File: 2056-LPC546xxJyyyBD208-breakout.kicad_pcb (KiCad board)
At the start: 2 copper layers, 99.1 x 99.1 mm, 149 parts, among them J1 0548190519, J10 Conn_01x03, J11 Conn_01x03, J12 Conn_01x03, J13 Conn_01x03, J14 Conn_01x03, J15 Conn_01x03, J16 Conn_01x03, J17 Conn_01x03, J18 Conn_01x03, J19 Conn_01x03, J2 Conn_01x03, J20 Conn_01x03, J21 Conn_01x03, J22 Conn_01x03, J23 Conn_01x03, J24 Conn_01x03, J25 Conn_01x03, J26 Conn_01x03, J27 Conn_01x03, J28 Conn_01x03, J29 Conn_01x03, J3 Conn_01x03, J30 Conn_02x01, J31 Conn_01x03, J32 Conn_01x04, J33 Conn_01x03, J34 TBL001-500-02GY-2GY, J35 Conn_02x05_Odd_Even, J36 Conn_01x03, J37 Conn_02x20_Odd_Even, J38 Conn_01x03, J39 Conn_01x03, J4 Conn_01x03, J40 Conn_01x03, J41 Conn_01x03, J42 Conn_01x03, J43 Conn_01x03, J5 Conn_01x03, J6 Conn_01x03, J7 Conn_01x03, J8 Conn_01x03, J9 Conn_01x03, Q2 ULN2803ADWR, Q3 ULN2803ADWR, SW1 SW_DIP_x08, U1 ST3232ECDR‎, U2 LPC546xxJyyyBD208, U3 SN65HVD232, U4 FAN8303, U5 FAN8303, U6 NCP1117ST50T3G, U7 FAN8303, Y1 12MHz

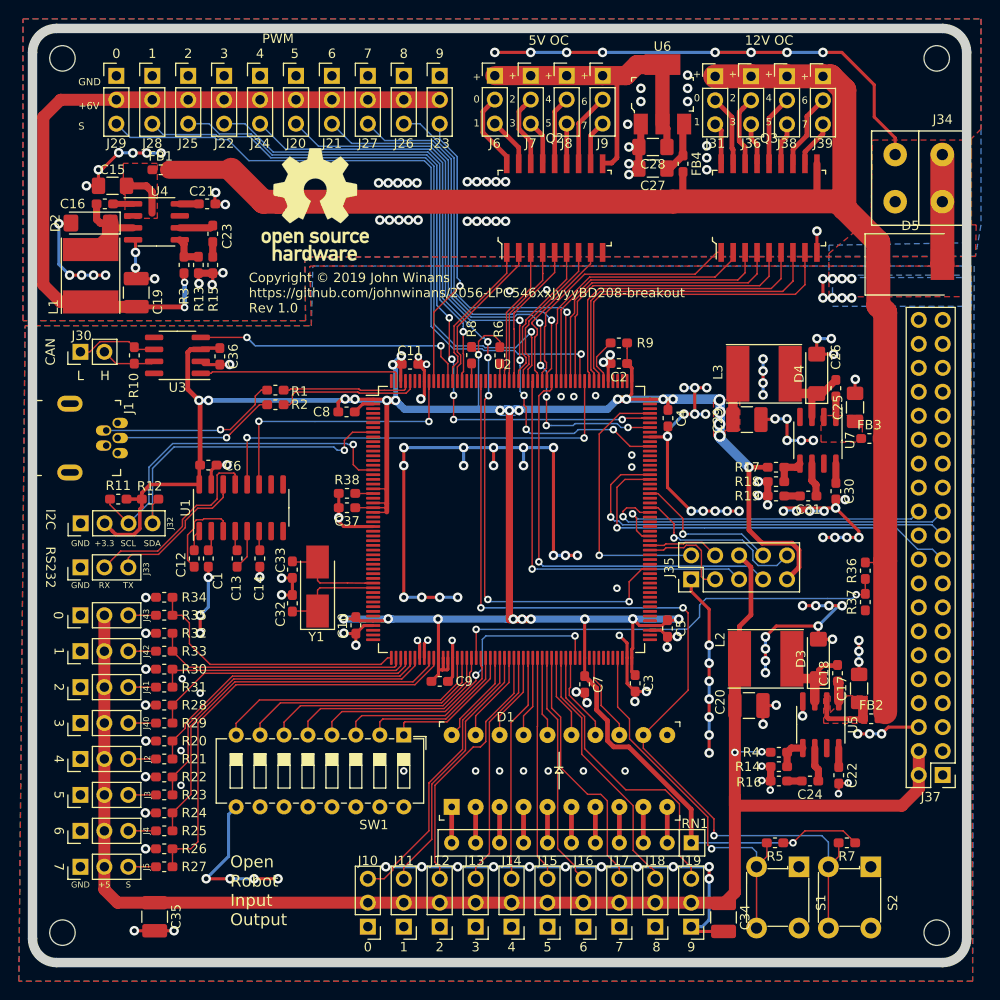
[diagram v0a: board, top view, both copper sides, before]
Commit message: Cosmetic silkscreen & title block cleanup.
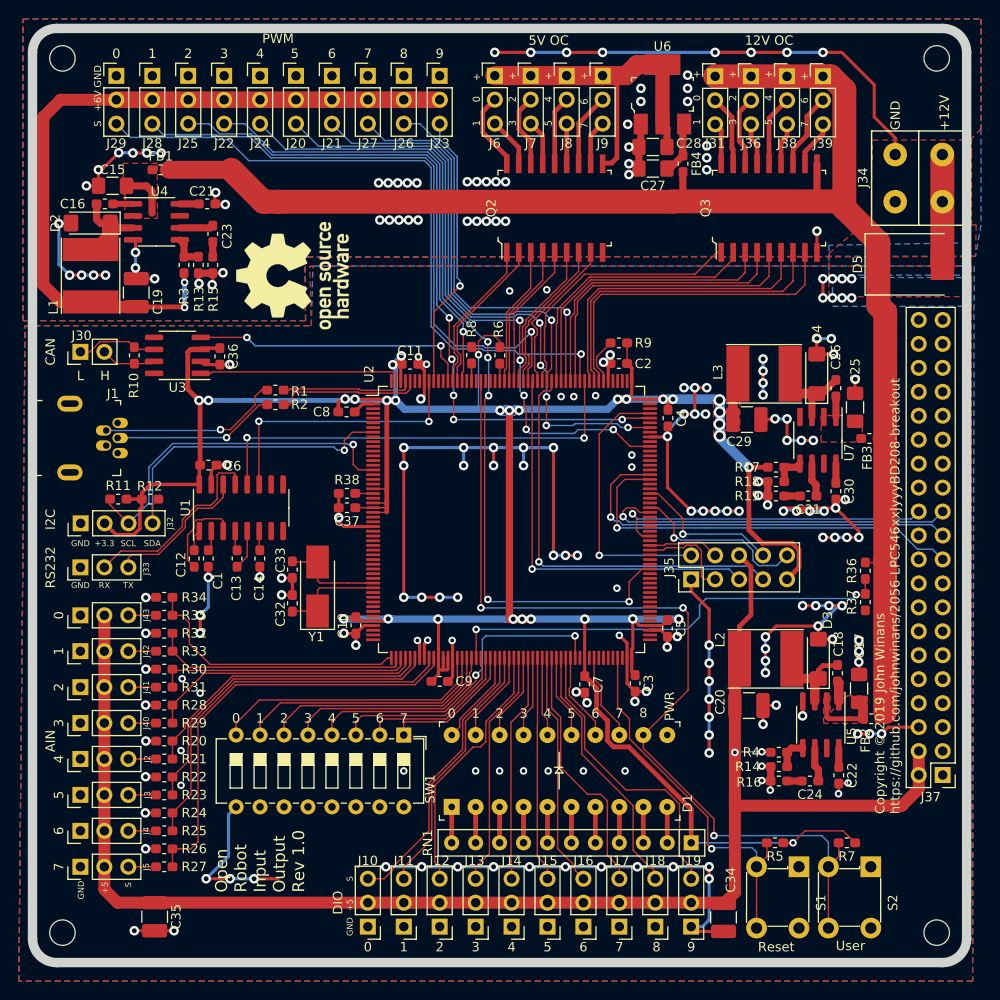
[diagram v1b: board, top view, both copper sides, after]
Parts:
- moved LOGO1 7.93 mm to (103.8, 77.0), turned to 90 degrees
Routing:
- net GND: vias 223 -> 222
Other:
- board text added: "+12V"
- board text added: "AIN"
- board text added: "Copyright © 2019 John Winans https://github.com/johnwinans/2056-LPC546xxJyyyBD208-breakout"
- board text added: "DIO"
- board text added: "Open Robot Input Output Rev 1.0"
- board text added: "PWR"
- board text added: "Reset"
- board text added: "User"
- board text removed: "Copyright © 2019 John Winans https://github.com/johnwinans/2056-LPC546xxJyyyBD208-breakout Rev 1.0"
- board text removed: "Open Robot Input Output"

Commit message: Rev 1.1 first manufacturable draft.
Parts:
- C23: value 146pF -> 390pF
- C24: value 146pF -> 560pF
- C31: value 146pF -> 820pF
- C32, C33: value 27pF -> 12pF
- L1, L2: value 15uH -> 22uH; footprint Inductor_SMD:L_Taiyo-Yuden_NR-60xx_HandSoldering -> Inductor_SMD:L_Taiyo-Yuden_NR-80xx_HandSoldering
- R13: value X -> 3K
- R14: value X -> 2K45
- R15: value 145K -> 56K
- R16: value 145K -> 43K
- R17, R3, R4: value X -> 18K
- R18: value X -> 4K
- R19: value 145K -> 27K
- U1: value ST3232ECDR‎ -> ST3232ECDR
- U2: value LPC546xxJyyyBD208 -> LPC54606J512BD208
- moved LOGO1 5.67 mm to (109.3, 78.0)
- moved C16 3.52 mm to (87.0, 67.9)
- moved C19 3.52 mm to (90.4, 77.3)
- moved C21 3.52 mm to (97.9, 67.9)
- moved C23 3.52 mm to (98.5, 71.1)
- moved D2 3.52 mm to (85.5, 69.9)
- moved FB1 3.52 mm to (93.0, 64.3)
- moved U4 3.52 mm to (92.5, 69.8)
- moved C15 3.52 mm to (87.9, 66.0)
- moved R13 3.52 mm to (97.0, 74.4)
- moved R15 3.52 mm to (98.5, 74.4)
- moved R3 3.52 mm to (95.4, 74.4)
- moved L1 2.17 mm to (84.5, 76.5)
- moved L2 1.49 mm to (152.9, 116.6)
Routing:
- net GND: track 448.1 -> 439.9 mm, vias 222 -> 219
- net +6V: track 79.5 -> 81.6 mm
- net +BATT: track 164.6 -> 163.4 mm
- net Net-(C21-Pad1): vias 0 -> 1
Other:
- board text added: "Open Robot Input Output Rev 1.1"
- board text removed: "Open Robot Input Output Rev 1.0"

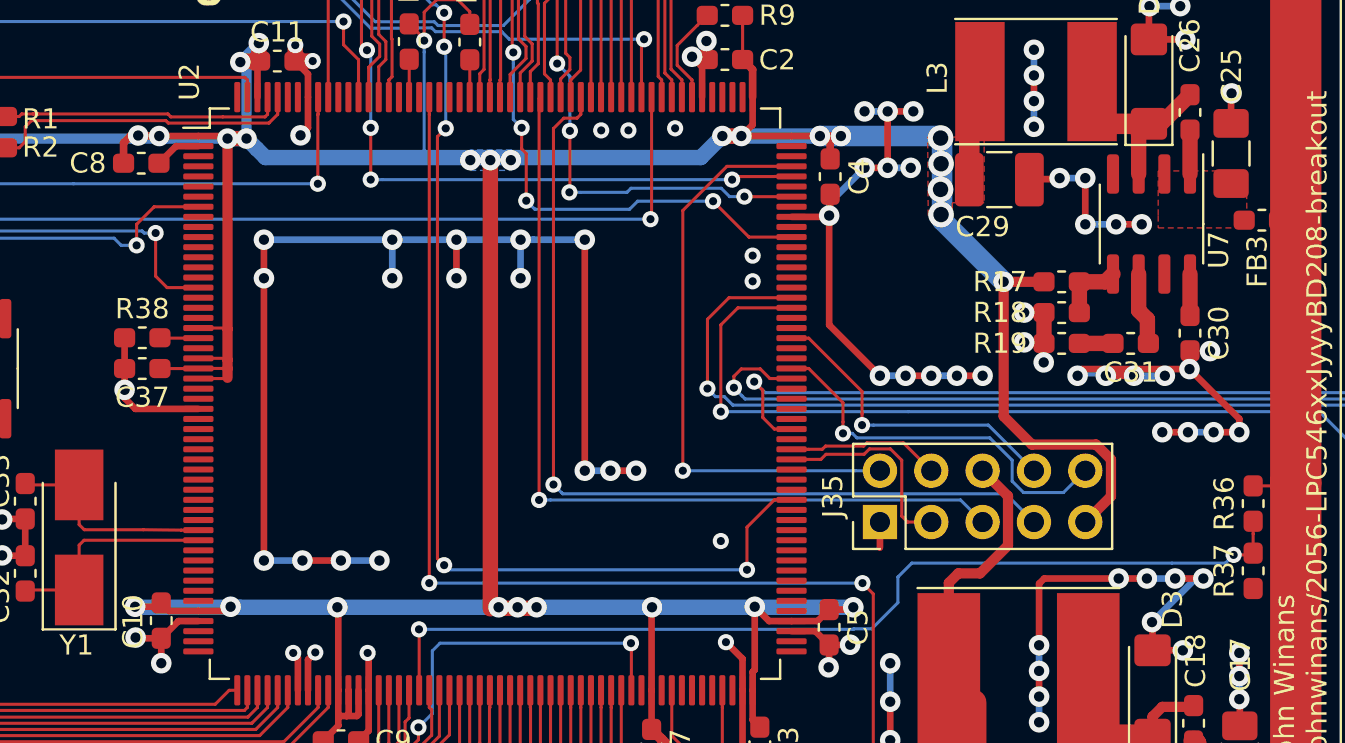
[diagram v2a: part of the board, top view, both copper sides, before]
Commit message: Correct CPU AVSSC pin.
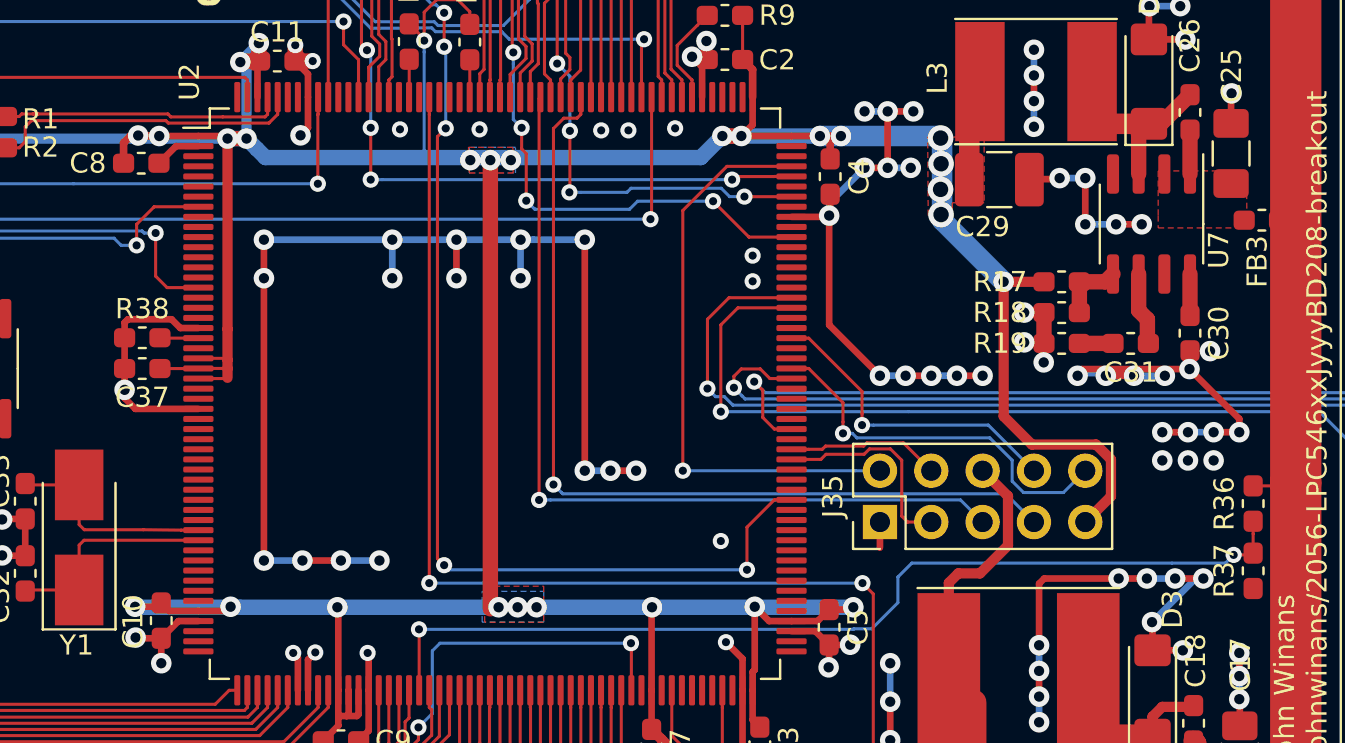
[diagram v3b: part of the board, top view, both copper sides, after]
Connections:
- U2 pad 20: +3V3 -> GND
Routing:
- net GND: track 439.9 -> 445.1 mm, vias 219 -> 224
- net +3V3: track 320.8 -> 317.1 mm
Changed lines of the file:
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@@
     (thickness 1.6)
     (drawings 115)
-    (tracks 1809)
+    (tracks 1817)
     (zones 0)
     (modules 149)
@@
     (pcbplotparams
       (layerselection 0x010fc_ffffffff)
-      (usegerberextensions false)
+      (usegerberextensions true)
       (usegerberattributes false)
       (usegerberadvancedattributes false)
@@
       (outputformat 1)
       (mirror false)
-      (drillshape 1)
+      (drillshape 0)
       (scaleselection 1)
-      (outputdirectory ""))
+      (outputdirectory "gerbers/"))
   )
   (net 0 "")
@@
       (net 293 "Net-(R38-Pad2)"))
     (pad 20 smd roundrect (at -14.675 -3.25) (size 1.5 0.3) (layers F.Cu F.Paste F.Mask) (roundrect_rratio 0.25)
-      (net 2 +3V3))
+      (net 1 GND))
     (pad 19 smd roundrect (at -14.675 -3.75) (size 1.5 0.3) (layers F.Cu F.Paste F.Mask) (roundrect_rratio 0.25)
       (net 244 "Net-(U2-Pad19)"))
@@
   (gr_line (start 175.26 53.34) (end 175.26 147.32) (layer Edge.Cuts) (width 1))
   (gr_line (start 78.74 50.8) (end 172.72 50.8) (layer Edge.Cuts) (width 1))
+  (via (at 162.56 106.172) (size 1.016) (drill 0.508) (layers F.Cu B.Cu) (net 1))
+  (via (at 161.29 106.172) (size 1.016) (drill 0.508) (layers F.Cu B.Cu) (net 1))
+  (via (at 160.02 106.172) (size 1.016) (drill 0.508) (layers F.Cu B.Cu) (net 1))
   (via (at 122.301 71.247) (size 1.016) (drill 0.508) (layers F.Cu B.Cu) (net 1))
   (via (at 122.301 67.056) (size 1.016) (drill 0.508) (layers F.Cu B.Cu) (net 1))
@@
   (segment (start 157.48 107.95) (end 157.48 106.1212) (width 0.508) (layer F.Cu) (net 2))
   (segment (start 152.1714 97.3328) (end 154.1666 97.3328) (width 0.508) (layer F.Cu) (net 2))
-  (segment (start 126.7996 113.4872) (end 129.0574 113.4872) (width 0.762) (layer F.Cu) (net 2))
   (segment (start 127.1792 113.4364) (end 126.46078 113.4364) (width 0.762) (layer B.Cu) (net 2))
   (segment (start 114.3762 113.4364) (end 109.2454 113.4364) (width 0.762) (layer B.Cu) (net 2))
@@
   (segment (start 113.693 101.12) (end 112.325 101.12) (width 0.1524) (layer F.Cu) (net 2))
   (segment (start 113.768 101.195) (end 113.768 101.624) (width 0.508) (layer F.Cu) (net 2))
-  (segment (start 113.717 99.62) (end 112.851 99.62) (width 0.1524) (layer F.Cu) (net 2))
   (segment (start 113.768 99.671) (end 113.717 99.62) (width 0.1524) (layer F.Cu) (net 2))
   (segment (start 113.768 90.2462) (end 113.768 99.671) (width 0.508) (layer F.Cu) (net 2))
   (segment (start 113.768 99.671) (end 113.768 101.195) (width 0.508) (layer F.Cu) (net 2))
-  (segment (start 112.851 99.62) (end 112.325 99.62) (width 0.1524) (layer F.Cu) (net 2))
+  (segment (start 112.851 99.62) (end 112.325 99.62) (width 0.1524) (layer F.Cu) (net 1))
+  (segment (start 112.325 99.62) (end 111.431 99.62) (width 0.3302) (layer F.Cu) (net 1))
+  (segment (start 111.431 99.62) (end 110.998 99.187) (width 0.3302) (layer F.Cu) (net 1))
+  (segment (start 110.998 99.187) (end 108.839 99.187) (width 0.3302) (layer F.Cu) (net 1))
+  (segment (start 108.6752 99.3508) (end 108.6752 100.1014) (width 0.3302) (layer F.Cu) (net 1))
+  (segment (start 108.839 99.187) (end 108.6752 99.3508) (width 0.3302) (layer F.Cu) (net 1))
+  (via (at 126.238 89.789) (size 0.8) (drill 0.4) (layers F.Cu B.Cu) (net 1))
+  (via (at 122.301 89.789) (size 0.8) (drill 0.4) (layers F.Cu B.Cu) (net 1))
   (segment (start 112.3196 101.6254) (end 112.325 101.62) (width 0.1524) (layer F.Cu) (net 2))
   (segment (start 110.4252 101.6254) (end 112.3196 101.6254) (width 0.1524) (layer F.Cu) (net 2))
@@
     )
   )
-  (zone (net 2) (net_name +3V3) (layer B.Cu) (hatch edge 0.508)
+  (zone (net 2) (net_name +3V3) (layer F.Cu) (hatch edge 0.508)
     (priority 2)
     (connect_pads yes (clearance 0.2032))
@@
     (polygon
       (pts
-        (xy 125.7808 90.805) (xy 125.7808 91.821) (xy 127.8382 91.821) (xy 127.8382 90.805)
+        (xy 125.6919 90.678) (xy 125.73 91.948) (xy 127.9017 91.948) (xy 127.889 90.678)
       )
     )
@@
       )
     )
+  )
+  (zone (net 2) (net_name +3V3) (layer F.Cu) (hatch edge 0.508)
+    (priority 2)
+    (connect_pads yes (clearance 0.2032))
+    (min_thickness 0.254)
+    (fill yes (arc_segments 32) (thermal_gap 0.254) (thermal_bridge_width 0.762))
+    (polygon
+      (pts
+        (xy 126.492 112.395) (xy 129.413 112.395) (xy 129.413 114.173) (xy 126.492 114.173)
+      )
+    )
+  )
+  (zone (net 2) (net_name +3V3) (layer B.Cu) (hatch edge 0.508)
+    (priority 2)
+    (connect_pads yes (clearance 0.2032))
+    (min_thickness 0.254)
+    (fill yes (arc_segments 32) (thermal_gap 0.254) (thermal_bridge_width 0.762))
+    (polygon
+      (pts
+        (xy 125.73 90.678) (xy 125.73 91.948) (xy 128.016 91.948) (xy 128.016 90.678)
+      )
+    )
+  )
+  (zone (net 2) (net_name +3V3) (layer B.Cu) (hatch edge 0.508)
+    (priority 2)
+    (connect_pads yes (clearance 0.2032))
+    (min_thickness 0.254)
+    (fill yes (arc_segments 32) (thermal_gap 0.254) (thermal_bridge_width 0.762))
+    (polygon
+      (pts
+        (xy 126.365 112.649) (xy 129.413 112.649) (xy 129.413 114.173) (xy 126.365 114.173)
+      )
+    )

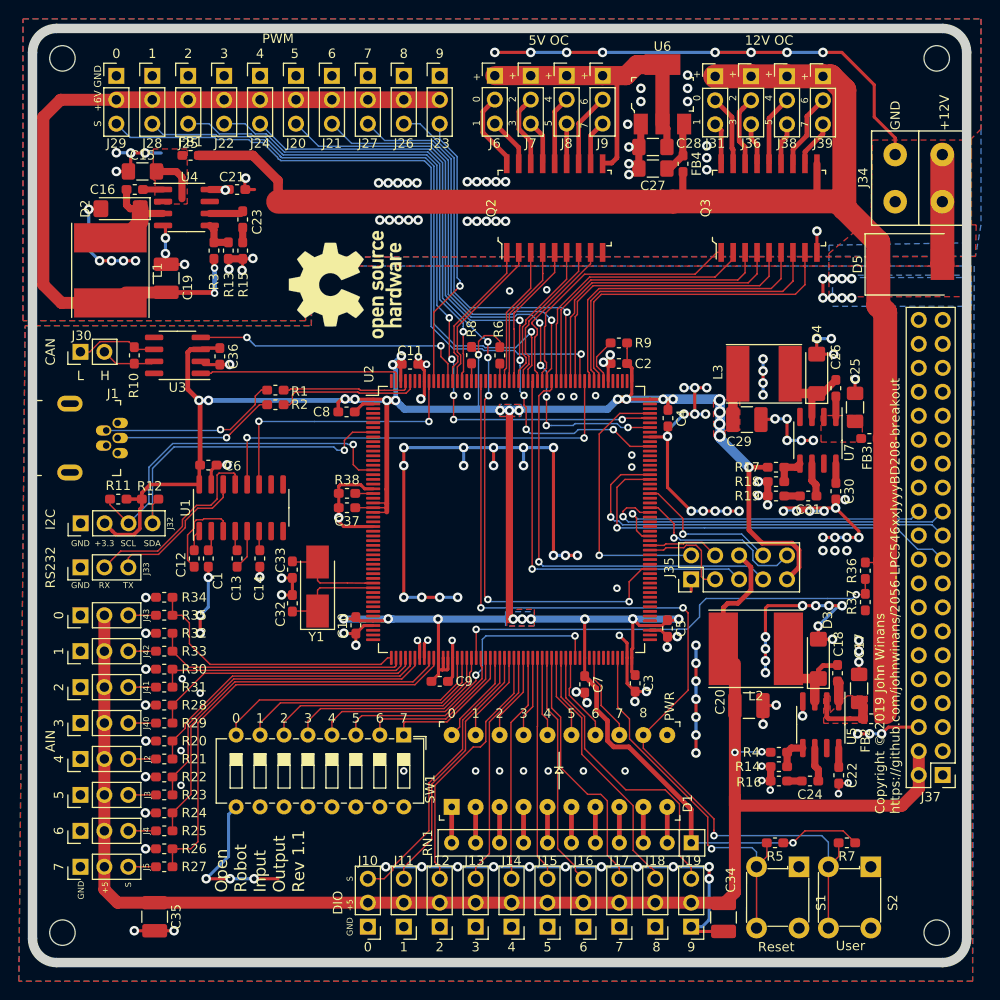
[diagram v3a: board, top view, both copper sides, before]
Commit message: Fixed power on VSSC pin, add filter caps, power & reset jumpers, SWD.
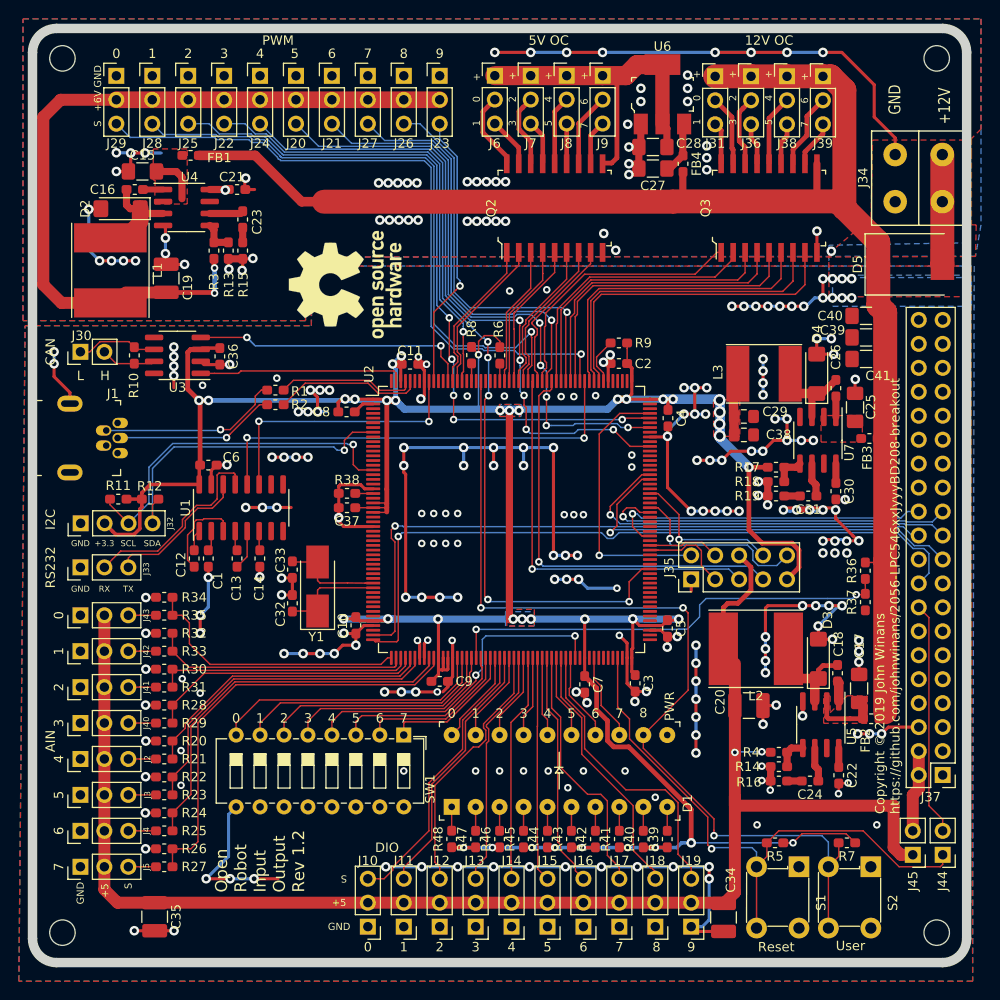
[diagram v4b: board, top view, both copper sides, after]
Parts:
- removed RN1: 330, Resistor_THT:R_Array_SIP11
- added C38: 22uF, Capacitor_SMD:C_0805_2012Metric_Pad1.15x1.40mm_HandSolder, F.Cu at (151.6, 93.9)
- added C39: 10uF, Capacitor_SMD:C_1206_3216Metric_Pad1.42x1.75mm_HandSolder, F.Cu at (164.6, 83.6)
- added C40: 10uF, Capacitor_SMD:C_1206_3216Metric_Pad1.42x1.75mm_HandSolder, F.Cu at (164.6, 81.3)
- added C41: 10uF, Capacitor_SMD:C_1206_3216Metric_Pad1.42x1.75mm_HandSolder, F.Cu at (164.6, 85.9)
- added J44: Conn_01x02, Connector_PinHeader_2.54mm:PinHeader_1x02_P2.54mm_Vertical, F.Cu at (172.7, 138.4)
- added J45: Conn_01x02, Connector_PinHeader_2.54mm:PinHeader_1x02_P2.54mm_Vertical, F.Cu at (169.5, 138.4)
- added R39: 330, Resistor_SMD:R_0603_1608Metric_Pad1.05x0.95mm_HandSolder, F.Cu at (143.5, 136.8)
- added R40: 330, Resistor_SMD:R_0603_1608Metric_Pad1.05x0.95mm_HandSolder, F.Cu at (141.0, 136.8)
- added R41: 330, Resistor_SMD:R_0603_1608Metric_Pad1.05x0.95mm_HandSolder, F.Cu at (138.4, 136.8)
- added R42: 330, Resistor_SMD:R_0603_1608Metric_Pad1.05x0.95mm_HandSolder, F.Cu at (135.9, 136.8)
- added R43: 330, Resistor_SMD:R_0603_1608Metric_Pad1.05x0.95mm_HandSolder, F.Cu at (133.3, 136.8)
- added R44: 330, Resistor_SMD:R_0603_1608Metric_Pad1.05x0.95mm_HandSolder, F.Cu at (130.8, 136.8)
- added R45: 330, Resistor_SMD:R_0603_1608Metric_Pad1.05x0.95mm_HandSolder, F.Cu at (128.3, 136.8)
- added R46: 330, Resistor_SMD:R_0603_1608Metric_Pad1.05x0.95mm_HandSolder, F.Cu at (125.7, 136.8)
- added R47: 330, Resistor_SMD:R_0603_1608Metric_Pad1.05x0.95mm_HandSolder, F.Cu at (123.2, 136.8)
- added R48: 330, Resistor_SMD:R_0603_1608Metric_Pad1.05x0.95mm_HandSolder, F.Cu at (120.7, 136.8)
- C29: footprint Capacitor_SMD:C_1210_3225Metric_Pad1.42x2.65mm_HandSolder -> Capacitor_SMD:C_0805_2012Metric_Pad1.15x1.40mm_HandSolder
- R13: value 3K -> 2K
- R20, R22, R24, R26, R28, R30, R32, R34: value 33K -> 5K
- R21, R23, R25, R27, R29, R31, R33, R35: value 27K -> 5K
- moved C29 0.46 mm to (151.6, 91.9)
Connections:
- J37 pad 18: Net-(J37-Pad18) -> /SWDIO
- J37 pad 2: +5V -> Net-(J37-Pad2)
- J37 pad 22: Net-(J37-Pad22) -> /SWCLK
- J37 pad 4: +5V -> Net-(J37-Pad2)
- U2 pad 51: Net-(U2-Pad51) -> /SWCLK
- U2 pad 52: Net-(U2-Pad52) -> /SWDIO
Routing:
- net /SWDIO: track 0.00 -> 75.3 mm, vias 0 -> 1
- net /SWCLK: track 0.00 -> 69.9 mm, vias 0 -> 1
- net GND: track 445.1 -> 513.6 mm, vias 224 -> 286
- net +3V3: track 317.1 -> 354.8 mm, vias 31 -> 39
- net Net-(J37-Pad16): track 0.00 -> 24.8 mm
- net /~RESET~: track 40.5 -> 62.3 mm
- net Net-(J37-Pad2): track 0.00 -> 8.72 mm
- net /FC6_MISO: track 44.0 -> 42.7 mm
- net +BATT: track 163.4 -> 162.1 mm
- net Net-(D1-Pad1): track 3.81 -> 2.53 mm
- net Net-(D1-Pad9): track 3.81 -> 2.54 mm
- net Net-(D1-Pad8): track 3.81 -> 2.54 mm
- net Net-(D1-Pad7): track 3.81 -> 2.54 mm
- net Net-(D1-Pad6): track 3.81 -> 2.54 mm
- net Net-(D1-Pad5): track 3.81 -> 2.54 mm
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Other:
- board text added: "Open Robot Input Output Rev 1.2"
- board text removed: "Open Robot Input Output Rev 1.1"
